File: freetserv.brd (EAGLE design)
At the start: 91.4 x 82.5 mm, 157 parts, among them IC1 MCP16311-E/MS, IC10 MAX3232ECPW, IC11 MAX3232ECPW, IC12 MAX3232ECPW, IC13 MAX3232ECPW, IC14 FT4232HL, IC15 MAX3232ECPW, IC16 MAX3232ECPW, IC17 MAX3232ECPW, IC18 MAX3232ECPW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

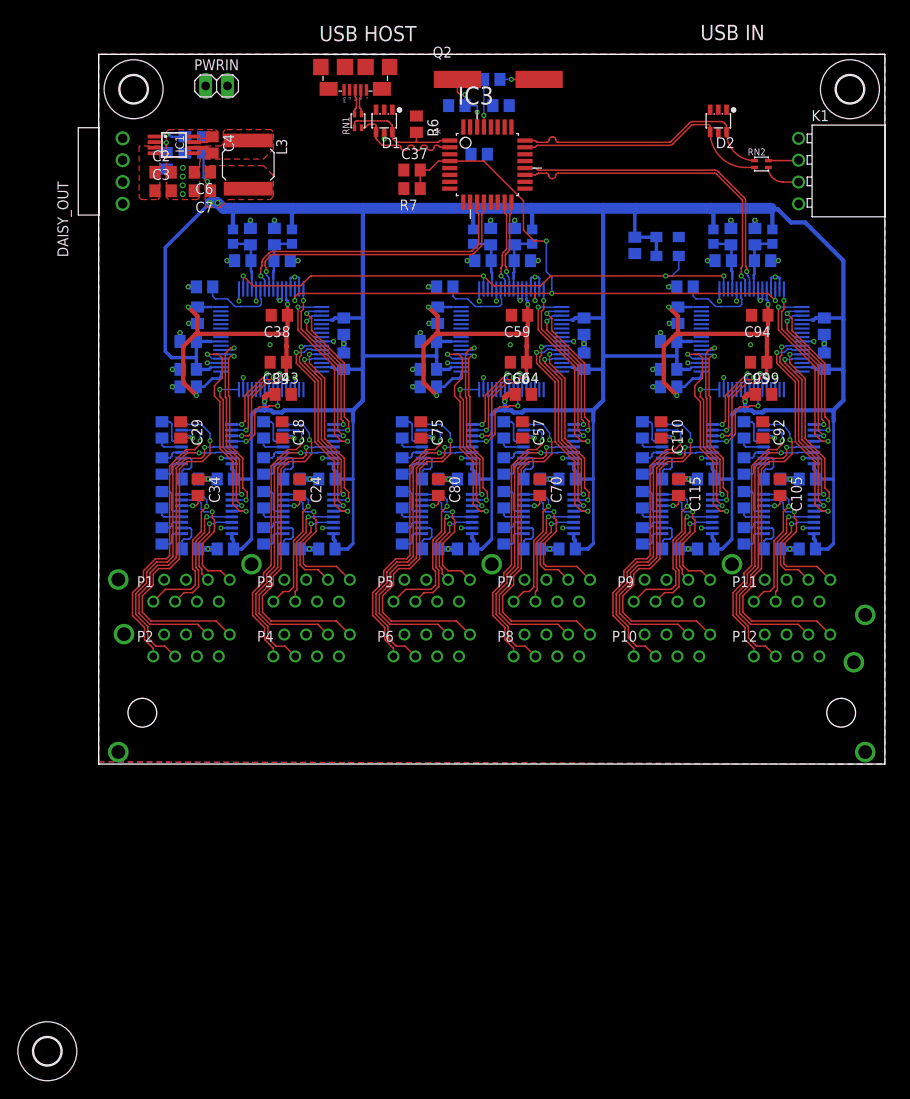
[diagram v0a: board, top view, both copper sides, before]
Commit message: fix drc warnings in power supply
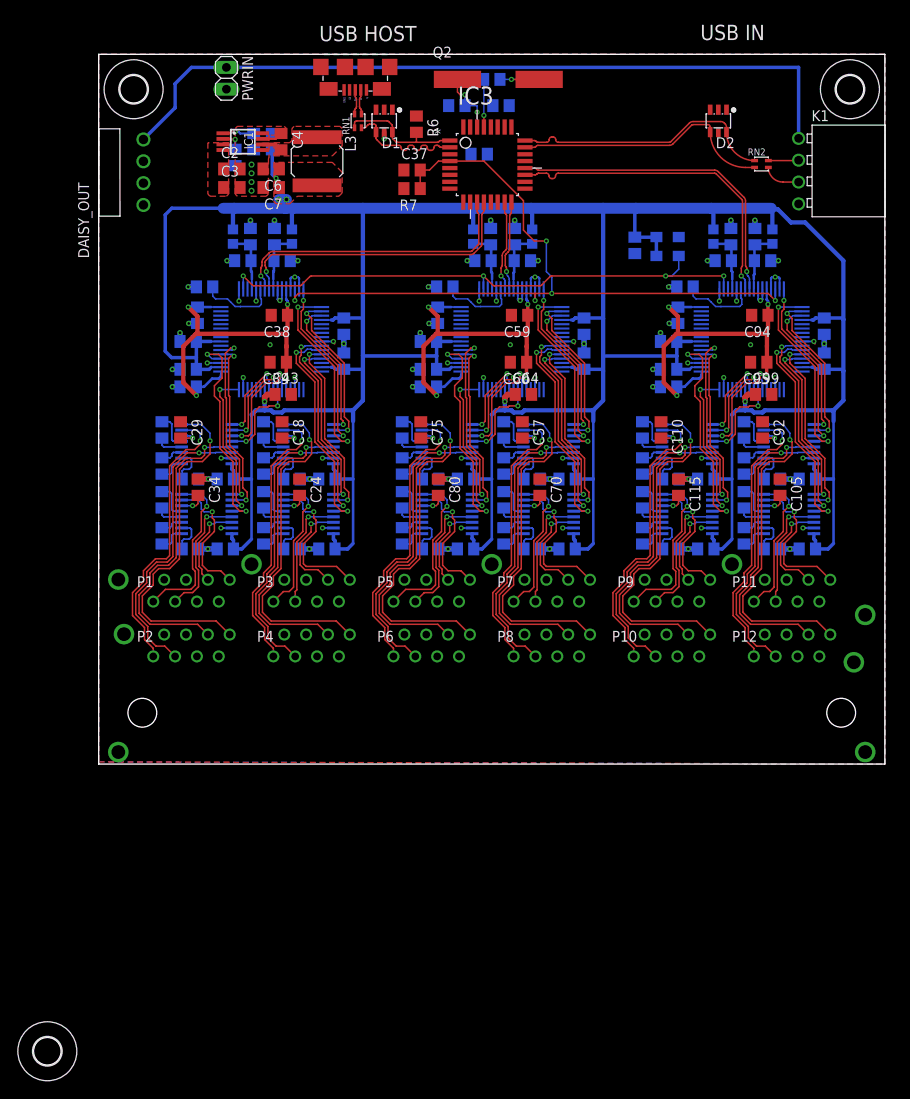
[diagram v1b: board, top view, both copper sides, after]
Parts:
- moved C5 8.01 mm to (15.9, 70.5)
- moved R4 8.01 mm to (20.2, 72.4)
- moved C2 8.01 mm to (15.5, 69.2)
- moved C3 8.01 mm to (15.5, 67.1)
- moved C4 8.01 mm to (21.2, 72.4)
- moved C6 8.01 mm to (20.1, 69.2)
- moved C7 8.01 mm to (20.1, 67.1)
- moved IC1 8.01 mm to (16.8, 72.4)
- moved R5 8.01 mm to (18.0, 72.4)
- moved L3 8.01 mm to (25.4, 70.1)
- moved DAISY_OUT 2.42 mm to (5.21, 68.8)
- moved PWRIN 1.45 mm to (14.9, 79.8), turned to 270 degrees
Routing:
- net +5V: track 0.66 -> 89.6 mm
- net +3V3: track 457.5 -> 461.2 mm

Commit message: wire up power supply
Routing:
- net +5V: track 89.6 -> 98.0 mm
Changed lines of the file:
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@@
 <contactref element="U$1" pad="P12.4"/>
 <contactref element="U$1" pad="P12.5"/>
-<polygon width="0.4064" layer="1">
+<polygon width="0.4064" layer="1" rank="6">
 <vertex x="0" y="82.55"/>
 <vertex x="0" y="0.254"/>
@@
 <contactref element="C6" pad="1"/>
 <contactref element="C7" pad="1"/>
-<polygon width="0.4064" layer="1" thermals="no" rank="2">
+<polygon width="0.4064" layer="1" thermals="no">
 <vertex x="20.3835" y="69.977"/>
 <vertex x="20.3835" y="65.405"/>
@@
 <contactref element="C2" pad="1"/>
 <contactref element="IC1" pad="4"/>
-<wire x1="14.544" y1="69.215" x2="14.714" y2="69.85" width="0" layer="19" extent="1-16"/>
-<polygon width="0.4064" layer="1" thermals="no" rank="2">
+<polygon width="0.4064" layer="1" thermals="no">
 <vertex x="15.113" y="66.294"/>
 <vertex x="15.113" y="72.263"/>
@@
 <wire x1="14.859" y1="81.026" x2="81.407" y2="81.026" width="0.4064" layer="16"/>
 <wire x1="81.407" y1="81.026" x2="81.407" y2="72.771" width="0.4064" layer="16"/>
-<wire x1="14.859" y1="81.026" x2="10.795" y2="81.026" width="0.4064" layer="16"/>
-<wire x1="10.795" y1="81.026" x2="8.89" y2="79.121" width="0.4064" layer="16"/>
-<wire x1="8.89" y1="79.121" x2="8.89" y2="76.327" width="0.4064" layer="16"/>
-<wire x1="8.89" y1="76.327" x2="5.207" y2="72.644" width="0.4064" layer="16"/>
-<wire x1="14.46" y1="72.065" x2="14.46" y2="71.415" width="0" layer="19" extent="1-1"/>
-<wire x1="14.714" y1="69.85" x2="14.46" y2="71.415" width="0" layer="19" extent="1-1"/>
-<wire x1="14.544" y1="67.056" x2="14.544" y2="69.215" width="0" layer="19" extent="1-1"/>
-<wire x1="8.89" y1="76.327" x2="14.46" y2="72.065" width="0" layer="19" extent="1-16"/>
+<wire x1="14.859" y1="81.026" x2="10.668" y2="81.026" width="0.4064" layer="1"/>
+<wire x1="10.668" y1="81.026" x2="9.525" y2="79.883" width="0.4064" layer="1"/>
+<wire x1="9.525" y1="79.883" x2="9.525" y2="76.962" width="0.4064" layer="1"/>
+<wire x1="9.525" y1="76.962" x2="5.207" y2="72.644" width="0.4064" layer="1"/>
+<wire x1="9.525" y1="76.962" x2="9.525" y2="75.057" width="0.4064" layer="1"/>
+<wire x1="9.525" y1="75.057" x2="13.208" y2="71.374" width="0.4064" layer="1"/>
+<wire x1="13.208" y1="71.374" x2="14.419" y2="71.374" width="0.4064" layer="1"/>
+<wire x1="14.419" y1="71.374" x2="14.46" y2="71.415" width="0.4064" layer="1"/>
 </signal>
 <signal name="N$3">
@@
 <wire x1="21.209" y1="71.44" x2="20.584" y2="72.065" width="0.254" layer="1"/>
 <wire x1="20.584" y1="72.065" x2="19.068" y2="72.065" width="0.45" layer="1"/>
-<polygon width="0.254" layer="1" thermals="no" rank="2">
+<polygon width="0.254" layer="1" thermals="no">
 <vertex x="20.3835" y="72.263"/>
 <vertex x="20.3835" y="70.739"/>

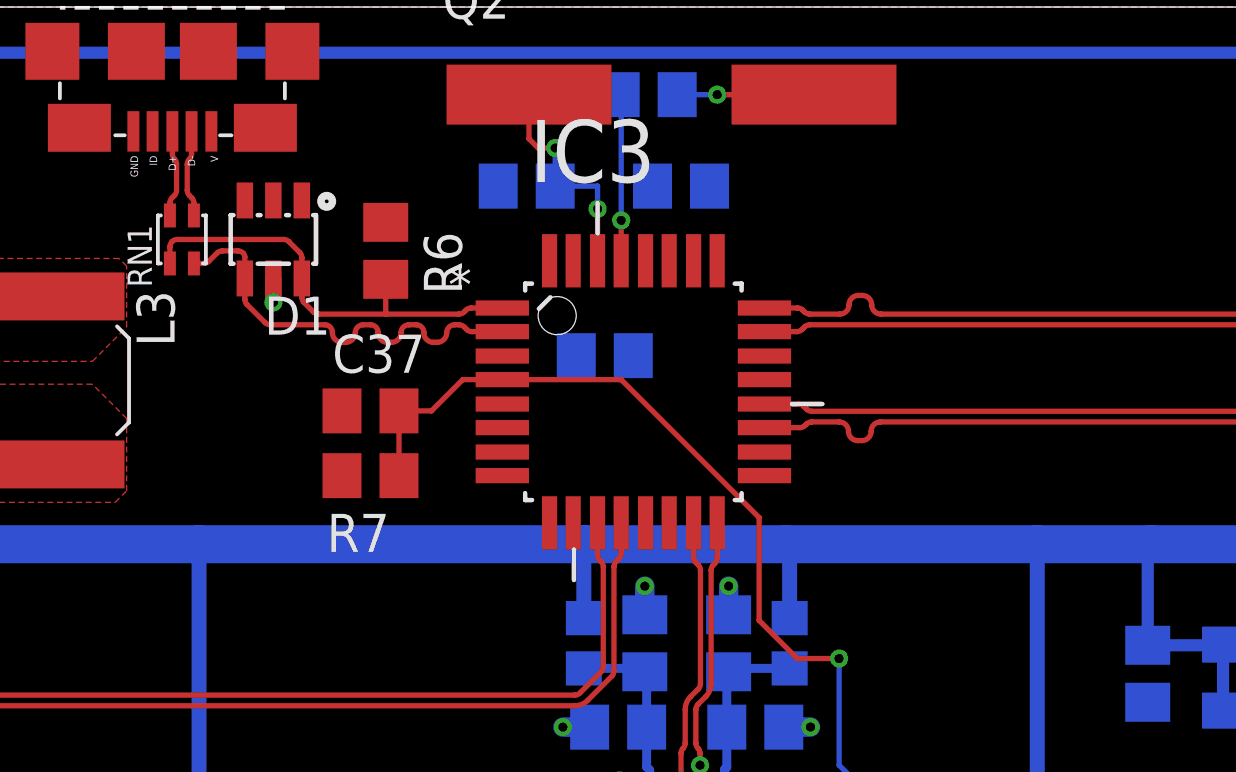
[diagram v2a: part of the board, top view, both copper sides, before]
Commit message: wire up USB hub
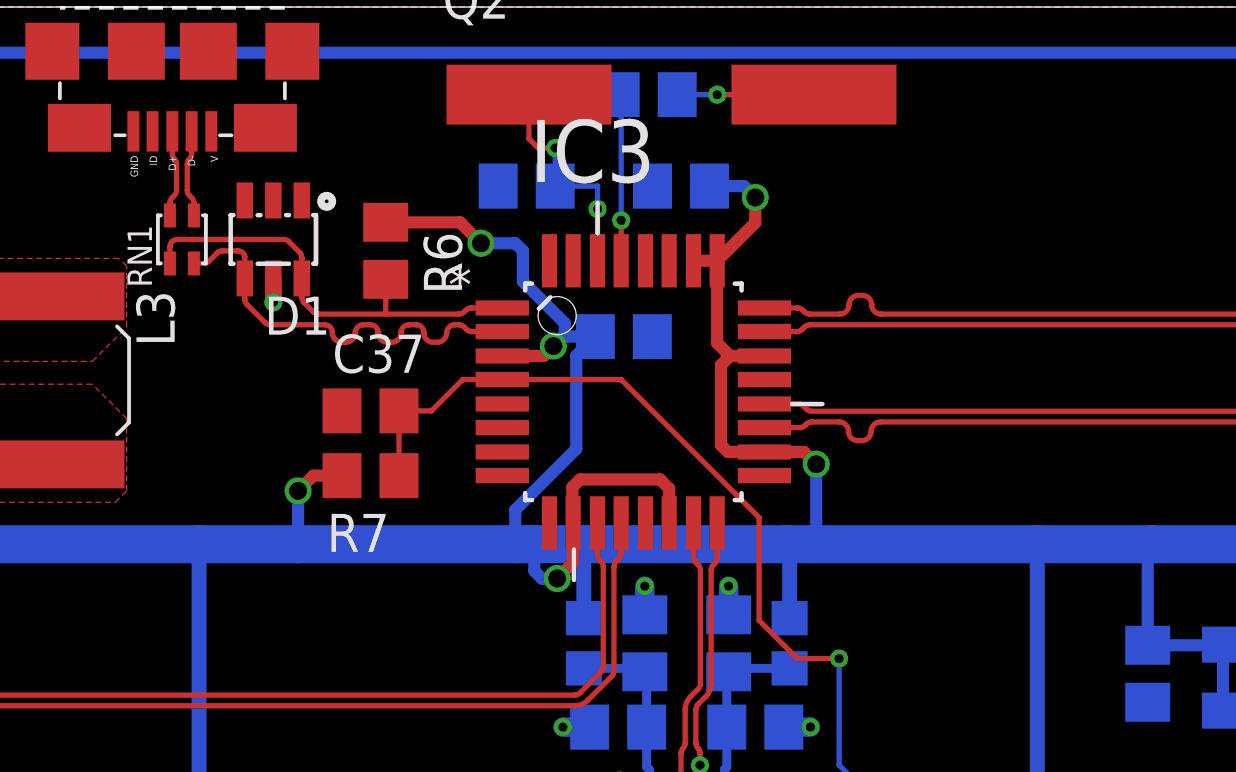
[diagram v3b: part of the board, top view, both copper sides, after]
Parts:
- moved C46 0.90 mm to (44.9, 71.6)
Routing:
- net +3V3: track 461.2 -> 513.0 mm, vias 6 -> 12
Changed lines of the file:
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@@
 <attribute name="OC_FARNELL" value="1470507" x="45.212" y="69.723" size="1.778" layer="27" display="off"/>
 </element>
-<element name="C46" library="resistor" package="C0805" value="0.1uF" x="44.2595" y="70.9295" rot="MR0">
-<attribute name="PARTNO" value="1276-1003-1-ND" x="44.2595" y="70.9295" size="1.778" layer="28" rot="MR0" display="off"/>
+<element name="C46" library="resistor" package="C0805" value="0.1uF" x="44.8945" y="71.5645" rot="MR0">
+<attribute name="PARTNO" value="1276-1003-1-ND" x="44.8945" y="71.5645" size="1.778" layer="28" rot="MR0" display="off"/>
 </element>
 <element name="IC6" library="Texas Instruments_By_element14_Batch_1" package="SOP65P640X120-16N" value="MAX3232ECPW" x="24.384" y="29.083" rot="MR180">
@@
 <wire x1="21.717" y1="64.643" x2="22.606" y2="64.643" width="1.27" layer="16"/>
 <wire x1="22.606" y1="64.643" x2="30.734" y2="64.643" width="1.27" layer="16"/>
-<wire x1="30.734" y1="64.643" x2="43.561" y2="64.643" width="1.27" layer="16"/>
+<wire x1="30.734" y1="64.643" x2="34.036" y2="64.643" width="1.27" layer="16"/>
+<wire x1="34.036" y1="64.643" x2="41.275" y2="64.643" width="1.27" layer="16"/>
+<wire x1="41.275" y1="64.643" x2="41.783" y2="64.643" width="1.27" layer="16"/>
+<wire x1="41.783" y1="64.643" x2="43.561" y2="64.643" width="1.27" layer="16"/>
 <wire x1="43.561" y1="64.643" x2="50.292" y2="64.643" width="1.27" layer="16"/>
-<wire x1="50.292" y1="64.643" x2="58.674" y2="64.643" width="1.27" layer="16"/>
+<wire x1="50.292" y1="64.643" x2="51.181" y2="64.643" width="1.27" layer="16"/>
+<wire x1="51.181" y1="64.643" x2="58.674" y2="64.643" width="1.27" layer="16"/>
 <wire x1="58.674" y1="64.643" x2="62.484" y2="64.643" width="1.27" layer="16"/>
 <wire x1="62.484" y1="64.643" x2="71.247" y2="64.643" width="1.27" layer="16"/>
@@
 <wire x1="21.844" y1="65.659" x2="21.717" y2="65.532" width="0.4064" layer="16"/>
 <wire x1="21.717" y1="65.532" x2="21.717" y2="64.643" width="0.4064" layer="16"/>
-<wire x1="48.006" y1="74.0918" x2="47.7495" y2="76.581" width="0" layer="19" extent="1-16"/>
-<wire x1="47.2186" y1="74.0918" x2="48.006" y2="74.0918" width="0" layer="19" extent="1-1"/>
-<wire x1="49.5808" y1="70.9168" x2="48.006" y2="74.0918" width="0" layer="19" extent="1-1"/>
-<wire x1="49.5808" y1="67.7164" x2="49.5808" y2="70.9168" width="0" layer="19" extent="1-1"/>
-<wire x1="50.292" y1="64.643" x2="49.5808" y2="67.7164" width="0" layer="19" extent="1-16"/>
-<wire x1="43.2054" y1="65.3542" x2="43.561" y2="64.643" width="0" layer="19" extent="1-16"/>
-<wire x1="46.4058" y1="65.3542" x2="43.561" y2="64.643" width="0" layer="19" extent="1-16"/>
-<wire x1="43.3095" y1="70.9295" x2="47.2186" y2="74.0918" width="0" layer="19" extent="1-16"/>
-<wire x1="40.8432" y1="70.9168" x2="43.3095" y2="70.9295" width="0" layer="19" extent="1-16"/>
-<wire x1="35.499" y1="66.929" x2="30.734" y2="64.643" width="0" layer="19" extent="1-16"/>
-<wire x1="36.957" y1="75.372" x2="40.8432" y2="70.9168" width="0" layer="19" extent="1-1"/>
+<wire x1="35.499" y1="66.929" x2="34.544" y2="66.929" width="0.4064" layer="1"/>
+<wire x1="34.544" y1="66.929" x2="34.036" y2="66.421" width="0.4064" layer="1"/>
+<via x="34.036" y="66.421" extent="1-16" drill="0.6"/>
+<wire x1="34.036" y1="66.421" x2="34.036" y2="64.643" width="0.4064" layer="16"/>
+<wire x1="49.5808" y1="67.7164" x2="50.9016" y2="67.7164" width="0.4064" layer="1"/>
+<wire x1="50.9016" y1="67.7164" x2="51.308" y2="67.31" width="0.4064" layer="1"/>
+<via x="51.308" y="67.31" extent="1-16" drill="0.6"/>
+<wire x1="51.308" y1="67.31" x2="51.308" y2="64.77" width="0.4064" layer="16"/>
+<wire x1="51.308" y1="64.77" x2="51.181" y2="64.643" width="0.4064" layer="16"/>
+<wire x1="49.5808" y1="67.7164" x2="48.3616" y2="67.7164" width="0.4064" layer="1"/>
+<wire x1="48.3616" y1="67.7164" x2="48.133" y2="67.945" width="0.4064" layer="1"/>
+<wire x1="48.133" y1="67.945" x2="48.133" y2="70.612" width="0.4064" layer="1"/>
+<wire x1="48.133" y1="70.612" x2="48.4378" y2="70.9168" width="0.4064" layer="1"/>
+<wire x1="48.4378" y1="70.9168" x2="49.5808" y2="70.9168" width="0.4064" layer="1"/>
+<wire x1="48.006" y1="74.0918" x2="48.006" y2="71.3486" width="0.4064" layer="1"/>
+<wire x1="48.006" y1="71.3486" x2="48.4378" y2="70.9168" width="0.4064" layer="1"/>
+<wire x1="47.2186" y1="74.0918" x2="48.006" y2="74.0918" width="0.4064" layer="1"/>
+<wire x1="43.2054" y1="65.3542" x2="43.2054" y2="64.0334" width="0.4064" layer="1"/>
+<wire x1="43.2054" y1="64.0334" x2="42.672" y2="63.5" width="0.4064" layer="1"/>
+<via x="42.672" y="63.5" extent="1-16" drill="0.6"/>
+<wire x1="42.672" y1="63.5" x2="42.164" y2="63.5" width="0.4064" layer="16"/>
+<wire x1="42.164" y1="63.5" x2="41.91" y2="63.754" width="0.4064" layer="16"/>
+<wire x1="41.91" y1="63.754" x2="41.91" y2="64.516" width="0.4064" layer="16"/>
+<wire x1="41.91" y1="64.516" x2="41.783" y2="64.643" width="0.4064" layer="16"/>
+<wire x1="46.4058" y1="65.3542" x2="46.4058" y2="66.4972" width="0.4064" layer="1"/>
+<wire x1="46.4058" y1="66.4972" x2="46.101" y2="66.802" width="0.4064" layer="1"/>
+<wire x1="46.101" y1="66.802" x2="43.434" y2="66.802" width="0.4064" layer="1"/>
+<wire x1="43.434" y1="66.802" x2="43.18" y2="66.548" width="0.4064" layer="1"/>
+<wire x1="43.18" y1="66.548" x2="43.18" y2="65.3796" width="0.4064" layer="1"/>
+<wire x1="43.18" y1="65.3796" x2="43.2054" y2="65.3542" width="0.4064" layer="1"/>
+<wire x1="43.3095" y1="67.8205" x2="41.275" y2="65.786" width="0.4064" layer="16"/>
+<wire x1="41.275" y1="65.786" x2="41.275" y2="64.643" width="0.4064" layer="16"/>
+<wire x1="43.3095" y1="67.8205" x2="43.3095" y2="70.9295" width="0.4064" layer="16"/>
+<wire x1="43.3095" y1="70.9295" x2="43.9445" y2="71.5645" width="0.4064" layer="16"/>
+<wire x1="43.9445" y1="71.5645" x2="42.926" y2="71.5645" width="0.4064" layer="16"/>
+<wire x1="42.926" y1="71.5645" x2="42.8625" y2="71.5645" width="0.4064" layer="16"/>
+<wire x1="42.8625" y1="71.5645" x2="42.545" y2="71.247" width="0.4064" layer="16"/>
+<via x="42.545" y="71.247" extent="1-16" drill="0.6"/>
+<wire x1="42.545" y1="71.247" x2="42.2148" y2="70.9168" width="0.4064" layer="1"/>
+<wire x1="42.2148" y1="70.9168" x2="40.8432" y2="70.9168" width="0.4064" layer="1"/>
+<wire x1="36.957" y1="75.372" x2="39.436" y2="75.372" width="0.4064" layer="1"/>
+<wire x1="39.436" y1="75.372" x2="40.132" y2="74.676" width="0.4064" layer="1"/>
+<via x="40.132" y="74.676" extent="1-16" drill="0.6"/>
+<wire x1="40.132" y1="74.676" x2="41.275" y2="74.676" width="0.4064" layer="16"/>
+<wire x1="41.275" y1="74.676" x2="41.529" y2="74.422" width="0.4064" layer="16"/>
+<wire x1="41.529" y1="74.422" x2="41.529" y2="73.406" width="0.4064" layer="16"/>
+<wire x1="41.529" y1="73.406" x2="42.926" y2="72.009" width="0.4064" layer="16"/>
+<wire x1="42.926" y1="72.009" x2="42.926" y2="71.5645" width="0.4064" layer="16"/>
+<wire x1="20.828" y1="67.056" x2="20.955" y2="65.659" width="0" layer="19" extent="1-1"/>
+<wire x1="21.016" y1="69.215" x2="20.193" y2="68.58" width="0" layer="19" extent="1-16"/>
+<wire x1="25.4" y1="67.304" x2="22.606" y2="64.643" width="0" layer="19" extent="1-16"/>
+<wire x1="47.7495" y1="76.581" x2="48.895" y2="76.581" width="0.4064" layer="16"/>
+<wire x1="48.895" y1="76.581" x2="49.276" y2="76.2" width="0.4064" layer="16"/>
+<via x="49.276" y="76.2" extent="1-16" drill="0.6"/>
+<wire x1="49.276" y1="76.2" x2="49.276" y2="75.3618" width="0.4064" layer="1"/>
+<wire x1="49.276" y1="75.3618" x2="48.006" y2="74.0918" width="0.4064" layer="1"/>
 </signal>
 <signal name="+5V" class="2">

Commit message: fix all airwires except from the USB differential pair
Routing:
- net GND: vias 86 -> 87
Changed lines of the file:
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@@
 <contactref element="PWRIN" pad="2"/>
 <contactref element="DAISY_OUT" pad="4"/>
-<wire x1="72.0725" y1="76.103" x2="72.0725" y2="73.503" width="0" layer="19" extent="1-1"/>
+<via x="72.0725" y="72.7075" extent="1-16" drill="0.3048"/>
 </signal>
 <signal name="+1V8-1">
@@
 <wire x1="41.529" y1="73.406" x2="42.926" y2="72.009" width="0.4064" layer="16"/>
 <wire x1="42.926" y1="72.009" x2="42.926" y2="71.5645" width="0.4064" layer="16"/>
-<wire x1="20.828" y1="67.056" x2="20.955" y2="65.659" width="0" layer="19" extent="1-1"/>
-<wire x1="21.016" y1="69.215" x2="20.193" y2="68.58" width="0" layer="19" extent="1-16"/>
-<wire x1="25.4" y1="67.304" x2="22.606" y2="64.643" width="0" layer="19" extent="1-16"/>
 <wire x1="47.7495" y1="76.581" x2="48.895" y2="76.581" width="0.4064" layer="16"/>
 <wire x1="48.895" y1="76.581" x2="49.276" y2="76.2" width="0.4064" layer="16"/>
@@
 <wire x1="10.6553" y1="38.1762" x2="10.922" y2="37.9095" width="0.2" layer="16"/>
 <via x="10.922" y="37.9095" extent="1-16" drill="0.3048"/>
-<wire x1="10.922" y1="37.9095" x2="9.5275" y2="37.9095" width="0.2" layer="1"/>
-<wire x1="9.5275" y1="37.9095" x2="9.525" y2="37.912" width="0" layer="19" extent="1-1"/>
+<wire x1="9.525" y1="37.912" x2="10.9195" y2="37.912" width="0.1778" layer="1"/>
+<wire x1="10.9195" y1="37.912" x2="10.922" y2="37.9095" width="0.1778" layer="1"/>
 </signal>
 <signal name="RXD3E">
@@
 <wire x1="38.5953" y1="38.1762" x2="38.862" y2="37.9095" width="0.2" layer="16"/>
 <via x="38.862" y="37.9095" extent="1-16" drill="0.3048"/>
-<wire x1="38.862" y1="37.9095" x2="37.4675" y2="37.9095" width="0.2" layer="1"/>
-<wire x1="37.4675" y1="37.9095" x2="37.465" y2="37.912" width="0" layer="19" extent="1-1"/>
+<wire x1="37.465" y1="37.912" x2="38.8595" y2="37.912" width="0.1778" layer="1"/>
+<wire x1="38.8595" y1="37.912" x2="38.862" y2="37.9095" width="0.1778" layer="1"/>
 </signal>
 <signal name="RXD3E1">
@@
 <wire x1="66.5353" y1="38.1762" x2="66.802" y2="37.9095" width="0.2" layer="16"/>
 <via x="66.802" y="37.9095" extent="1-16" drill="0.3048"/>
-<wire x1="66.802" y1="37.9095" x2="65.4075" y2="37.9095" width="0.2" layer="1"/>
-<wire x1="65.4075" y1="37.9095" x2="65.405" y2="37.912" width="0" layer="19" extent="1-1"/>
+<wire x1="65.405" y1="37.912" x2="66.7995" y2="37.912" width="0.1778" layer="1"/>
+<wire x1="66.7995" y1="37.912" x2="66.802" y2="37.9095" width="0.1778" layer="1"/>
 </signal>
 <signal name="RXD3E2">
@@
 <contactref element="K1" pad="4"/>
 </signal>
+<signal name="N$16">
+</signal>
 </signals>
